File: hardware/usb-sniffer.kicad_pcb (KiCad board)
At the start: 2 copper layers, 58.2 x 38.1 mm, 87 parts, among them IC1 LCMXO2-2000HC-5TG100, IC10 DSC6101CI2A-024.0000, IC2 MIC5504-3.3v, IC3 MAX9032AKA+T, IC4 USB3343, IC5 MAX9032AKA+T, IC6 DSC6101CI2A-026.0000, IC7 MAX9032AKA+T, IC8 24LC128, IC9 CY7C68013A-56PVXC, J1 USB-C, J2 USB-C, J3 USB-A, J4 IN, J5 GND

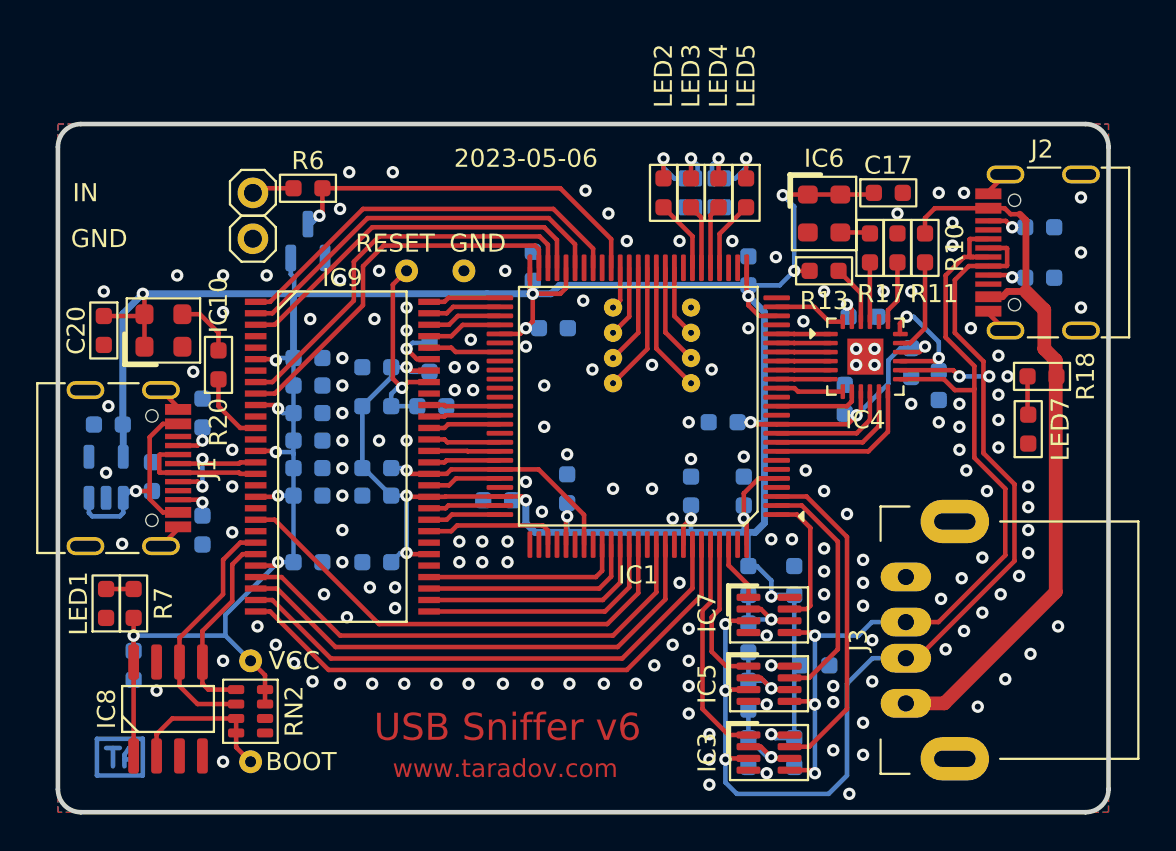
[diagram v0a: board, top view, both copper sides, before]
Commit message: replace obsolete components, updated PCB, schematics and production files
Signed-off-by: Jakub Sobota <jakub.sobota@3mdeb.com>
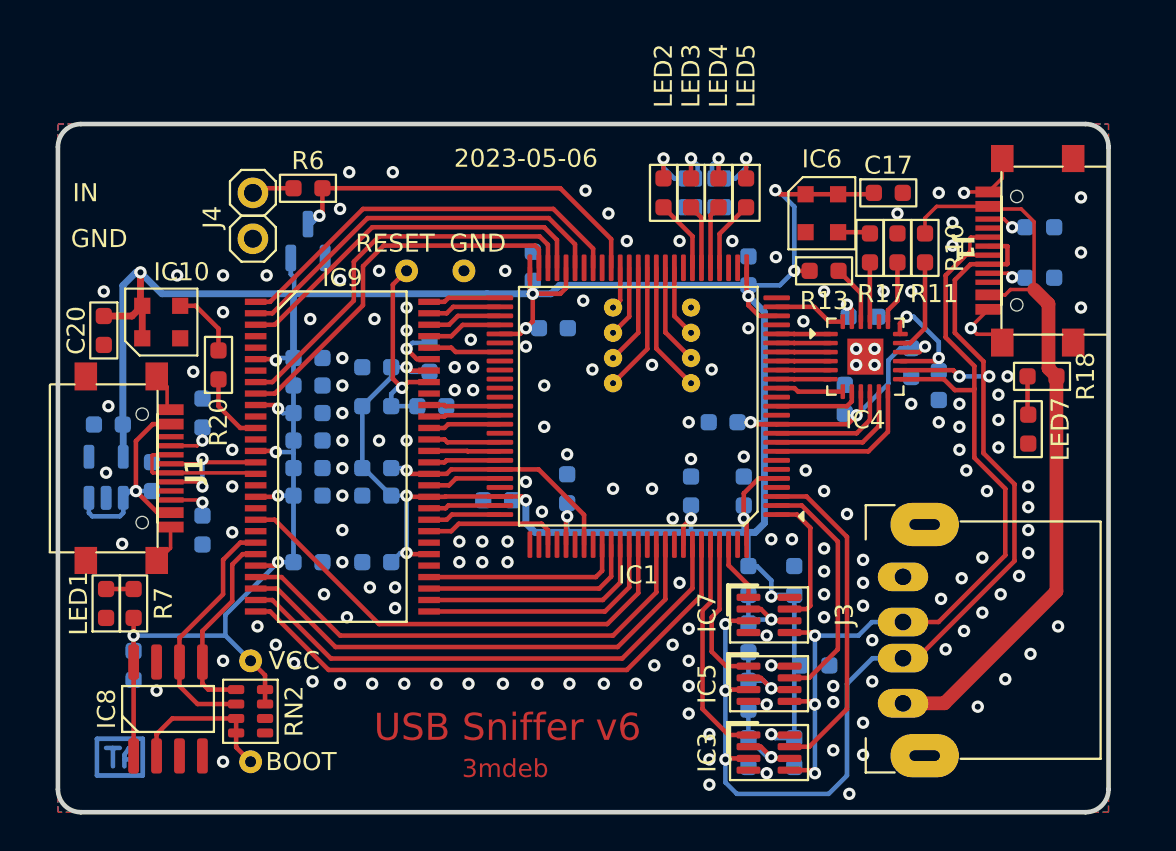
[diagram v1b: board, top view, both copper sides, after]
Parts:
- removed the J1 at (22.5, 48.4)
- removed J2: USB-C, ataradov_conn:USB-C
- added J1: USBC-F, USB Connectors:USBC-F, F.Cu at (35.0, 52.2)
- added J1: USBC-F, USB Connectors:USBC-F, F.Cu at (64.6, 32.5)
- IC10: value DSC6101CI2A-024.0000 -> 3.2 mm x 2.5 mm; footprint ataradov_ic:CDFN-4-3.2x2.5mm -> Oscilator:3.2 mm x 2.5 mm
- IC6: value DSC6101CI2A-026.0000 -> 3.2 mm x 2.5 mm; footprint ataradov_ic:CDFN-4-3.2x2.5mm -> Oscilator:3.2 mm x 2.5 mm
- IC9: value CY7C68013A-56PVXC -> CBM9002A-56ISG
- J3: value USB-A -> USB-A_F; footprint ataradov_conn:USB-A-Slots -> USB Connectors:USB-A_F
- moved J3 8.25 mm to (78.5, 60.4), turned to 0 degrees
- moved IC10 0.48 mm to (26.7, 40.3)
- moved IC6 0.12 mm to (63.2, 34.3)
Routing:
- net GND: track 5.86 -> 11.3 mm, vias 166 -> 165
- net /Host USB/DP: track 7.30 -> 11.5 mm
- net +3V3: track 223.9 -> 227.9 mm
- net /T_USB_DP: track 50.7 -> 52.3 mm
- net /T_USB_VBUS: track 41.3 -> 42.2 mm
- net /T_USB_DM: track 64.5 -> 65.4 mm
- net Net-(J1-PadCC2): track 1.41 -> 2.04 mm
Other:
- board text added: "3mdeb"
- board text added: "J4"
- board text removed: "www.taradov.com"
